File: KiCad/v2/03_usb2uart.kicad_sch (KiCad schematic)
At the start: 35 parts, among them IC301 CP2102N-A02-GQFN24R, J301 Conn_01x09_Pin, J302 Conn_01x09_Pin, J303 Conn_01x06_Pin, J304 USB_C_Receptacle_USB2.0_16P, J305 Conn_01x03_Pin, U301 USBLC6-2SC6

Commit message: Initial components placement
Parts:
- C301, C303, C304, C307, C310: footprint Capacitor_SMD:C_0603_1608Metric -> Capacitor_SMD:C_0402_1005Metric
- C302, C305, C306: footprint Capacitor_SMD:C_0805_2012Metric -> Capacitor_SMD:C_0603_1608Metric
- C311: footprint Capacitor_SMD:C_0603_1608Metric -> Capacitor_SMD:C_0402_1005Metric; now not fitted; now left out of the parts list
- SW301: now not fitted; now left out of the parts list
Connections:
- net RS485: now also J301.9 (Pin_9); no longer J301.7 (Pin_7)
- net RSTB: now also J301.7 (Pin_7); no longer J301.9 (Pin_9)
- net USB_CONN_D+: now also U301.3 (I/O2); no longer U301.1 (I/O1)
- net USB_CONN_D-: now also U301.1 (I/O1); no longer U301.3 (I/O2)
- net USB_D+: now also U301.4 (I/O2); no longer U301.6 (I/O1)
- net USB_D-: now also U301.6 (I/O1); no longer U301.4 (I/O2)
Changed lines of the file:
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@@
 	)
 	(junction
-		(at 48.26 99.06)
-		(diameter 0)
-		(color 0 0 0 0)
-	)
-	(junction
 		(at 184.15 59.69)
 		(diameter 0)
@@
 	)
 	(junction
-		(at 21.59 184.15)
+		(at 48.26 99.06)
 		(diameter 0)
 		(color 0 0 0 0)
 	)
 	(junction
-		(at 175.26 59.69)
+		(at 21.59 184.15)
 		(diameter 0)
 		(color 0 0 0 0)
 	)
 	(junction
-		(at 48.26 104.14)
+		(at 175.26 59.69)
 		(diameter 0)
 		(color 0 0 0 0)
@@
 	)
 	(junction
+		(at 48.26 101.6)
+		(diameter 0)
+		(color 0 0 0 0)
+	)
+	(junction
 		(at 151.13 39.37)
 		(diameter 0)
@@
 	(wire
 		(pts
-			(xy 53.34 99.06) (xy 48.26 99.06)
-		)
-		(stroke
-			(width 0)
-			(type default)
-		)
-	)
-	(wire
-		(pts
 			(xy 242.57 88.9) (xy 255.27 88.9)
 		)
@@
 	(wire
 		(pts
-			(xy 139.7 168.91) (xy 139.7 172.72)
+			(xy 115.57 101.6) (xy 120.65 101.6)
 		)
 		(stroke
@@
 	(wire
 		(pts
-			(xy 115.57 101.6) (xy 120.65 101.6)
+			(xy 139.7 168.91) (xy 139.7 172.72)
 		)
 		(stroke
@@
 	(wire
 		(pts
-			(xy 53.34 101.6) (xy 53.34 99.06)
-		)
-		(stroke
-			(width 0)
-			(type default)
-		)
-	)
-	(wire
-		(pts
 			(xy 41.91 78.74) (xy 48.26 78.74)
 		)
@@
 	(wire
 		(pts
+			(xy 115.57 99.06) (xy 120.65 99.06)
+		)
+		(stroke
+			(width 0)
+			(type default)
+		)
+	)
+	(wire
+		(pts
 			(xy 185.42 81.28) (xy 191.77 81.28)
 		)
@@
 	(wire
 		(pts
-			(xy 105.41 99.06) (xy 80.01 99.06)
-		)
-		(stroke
-			(width 0)
-			(type default)
-		)
-	)
-	(wire
-		(pts
-			(xy 80.01 99.06) (xy 80.01 104.14)
+			(xy 53.34 91.44) (xy 53.34 68.58)
 		)
 		(stroke
@@
 	(wire
 		(pts
-			(xy 53.34 91.44) (xy 53.34 68.58)
+			(xy 46.99 96.52) (xy 48.26 96.52)
 		)
 		(stroke
@@
 	(wire
 		(pts
-			(xy 46.99 96.52) (xy 48.26 96.52)
+			(xy 76.2 161.29) (xy 76.2 157.48)
 		)
 		(stroke
@@
 	(wire
 		(pts
-			(xy 76.2 161.29) (xy 76.2 157.48)
+			(xy 48.26 101.6) (xy 105.41 101.6)
 		)
 		(stroke
@@
 	(wire
 		(pts
-			(xy 115.57 99.06) (xy 120.65 99.06)
-		)
-		(stroke
-			(width 0)
-			(type default)
-		)
-	)
-	(wire
-		(pts
 			(xy 139.7 181.61) (xy 139.7 177.8)
 		)
@@
 	(wire
 		(pts
-			(xy 48.26 104.14) (xy 80.01 104.14)
+			(xy 48.26 99.06) (xy 105.41 99.06)
 		)
 		(stroke
@@
 	(wire
 		(pts
-			(xy 53.34 101.6) (xy 105.41 101.6)
-		)
-		(stroke
-			(width 0)
-			(type default)
-		)
-	)
-	(wire
-		(pts
 			(xy 158.75 48.26) (xy 158.75 49.53)
 		)
@@
 	)
 	(label "USB_CONN_D+"
-		(at 71.12 104.14 180)
+		(at 71.12 101.6 180)
 		(effects
 			(font
@@
 		)
 	)
-	(label "RSTB"
-		(at 247.65 45.72 0)
-		(effects
-			(font
-				(size 1.27 1.27)
-			)
-			(justify left bottom)
-		)
-	)
 	(label "WAKEUP"
 		(at 247.65 38.1 0)
@@
 	)
 	(label "USB_CONN_D-"
-		(at 71.12 101.6 180)
+		(at 71.12 99.06 180)
 		(effects
 			(font
@@
 		)
 	)
+	(label "RS485"
+		(at 247.65 45.72 0)
+		(effects
+			(font
+				(size 1.27 1.27)
+			)
+			(justify left bottom)
+		)
+	)
 	(label "DCD"
 		(at 246.38 77.47 0)
@@
 		)
 	)
+	(label "RSTB"
+		(at 247.65 40.64 0)
+		(effects
+			(font
+				(size 1.27 1.27)
+			)
+			(justify left bottom)
+		)
+	)
 	(label "RTS"
 		(at 246.38 62.23 0)
@@
 		)
 	)
-	(label "RS485"
-		(at 247.65 40.64 0)
-		(effects
-			(font
-				(size 1.27 1.27)
-			)
-			(justify left bottom)
-		)
-	)
 	(label "USB_CONN_CC1"
 		(at 69.85 64.77 180)
@@
 	(global_label "USB_D-"
 		(shape input)
-		(at 120.65 101.6 0)
+		(at 120.65 99.06 0)
 		(fields_autoplaced yes)
 		(effects
@@
 		)
 		(property "Intersheetrefs" "${INTERSHEET_REFS}"
-			(at 131.2552 101.6 0)
+			(at 131.2552 99.06 0)
 			(effects
 				(font
@@
 	(global_label "USB_D+"
 		(shape input)
-		(at 120.65 99.06 0)
+		(at 120.65 101.6 0)
 		(fields_autoplaced yes)
 		(effects
@@
 		)
 		(property "Intersheetrefs" "${INTERSHEET_REFS}"
-			(at 131.2552 99.06 0)
+			(at 131.2552 101.6 0)
 			(effects
 				(font
@@
 			)
 		)
-		(property "Footprint" "Capacitor_SMD:C_0805_2012Metric"
+		(property "Footprint" "Capacitor_SMD:C_0603_1608Metric"
 			(at 185.1152 68.58 0)
 			(effects
@@
 			)
 		)
-		(property "Footprint" "Capacitor_SMD:C_0603_1608Metric"
+		(property "Footprint" "Capacitor_SMD:C_0402_1005Metric"
 			(at 154.6352 69.85 0)
 			(effects
@@
 			)
 		)
-		(property "Footprint" "Capacitor_SMD:C_0603_1608Metric"
+		(property "Footprint" "Capacitor_SMD:C_0402_1005Metric"
 			(at 176.2252 43.18 0)
 			(effects
@@
 		(at 132.08 173.99 0)
 		(unit 1)
-		(exclude_from_sim no)
-		(in_bom yes)
-		(on_board yes)
-		(dnp no)
+		(exclude_from_sim yes)
+		(in_bom no)
+		(on_board no)
+		(dnp yes)
 		(property "Reference" "SW301"
 			(at 132.08 170.18 0)
@@
 			)
 		)
-		(property "Footprint" "Capacitor_SMD:C_0603_1608Metric"
+		(property "Footprint" "Capacitor_SMD:C_0402_1005Metric"
 			(at 95.25 87.3252 0)
 			(effects
@@
 			)
 		)
-		(property "Footprint" "Capacitor_SMD:C_0805_2012Metric"
+		(property "Footprint" "Capacitor_SMD:C_0603_1608Metric"
 			(at 185.1152 43.18 0)
 			(effects
@@
 		(at 116.84 177.8 0)
 		(unit 1)
-		(exclude_from_sim no)
-		(in_bom yes)
-		(on_board yes)
-		(dnp no)
+		(exclude_from_sim yes)
+		(in_bom no)
+		(on_board no)
+		(dnp yes)
 		(property "Reference" "C311"
 			(at 117.602 175.006 0)
@@
 			)
 		)
-		(property "Footprint" "Capacitor_SMD:C_0603_1608Metric"
+		(property "Footprint" "Capacitor_SMD:C_0402_1005Metric"
 			(at 117.8052 181.61 0)
 			(effects
@@
 			)
 		)
-		(property "Footprint" "Capacitor_SMD:C_0603_1608Metric"
+		(property "Footprint" "Capacitor_SMD:C_0402_1005Metric"
 			(at 159.7152 48.26 0)
 			(effects
@@
 			)
 		)
-		(property "Footprint" "Capacitor_SMD:C_0805_2012Metric"
+		(property "Footprint" "Capacitor_SMD:C_0603_1608Metric"
 			(at 144.4752 69.85 0)
 			(effects
@@
 			)
 		)
-		(property "Footprint" "Capacitor_SMD:C_0603_1608Metric"
+		(property "Footprint" "Capacitor_SMD:C_0402_1005Metric"
 			(at 176.2252 68.58 0)
 			(effects

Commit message: initial routing
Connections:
- net USB_CONN_D+: now also U301.1 (I/O1); no longer U301.3 (I/O2)
- net USB_CONN_D-: now also U301.3 (I/O2); no longer U301.1 (I/O1)
- net USB_D+: now also U301.6 (I/O1); no longer U301.4 (I/O2)
- net USB_D-: now also U301.4 (I/O2); no longer U301.6 (I/O1)

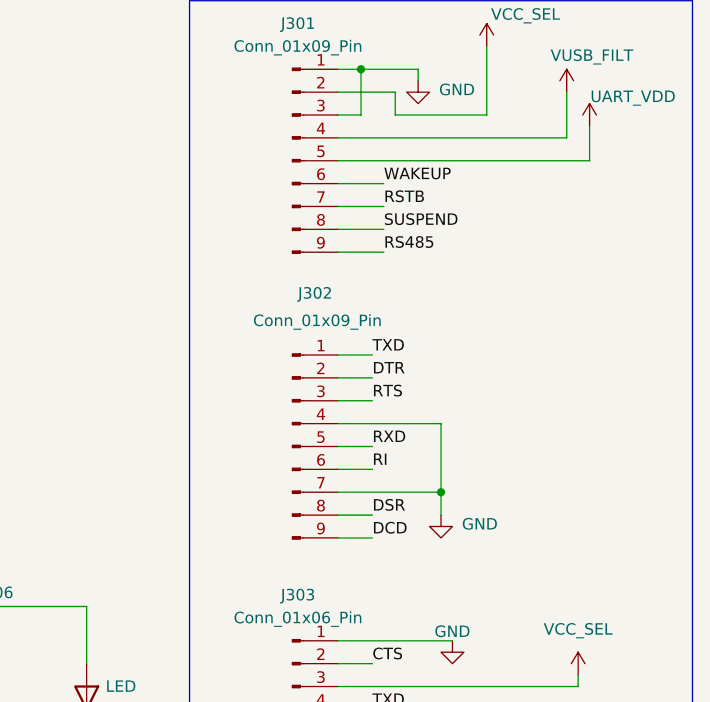
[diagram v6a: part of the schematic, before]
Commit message: Signal routing
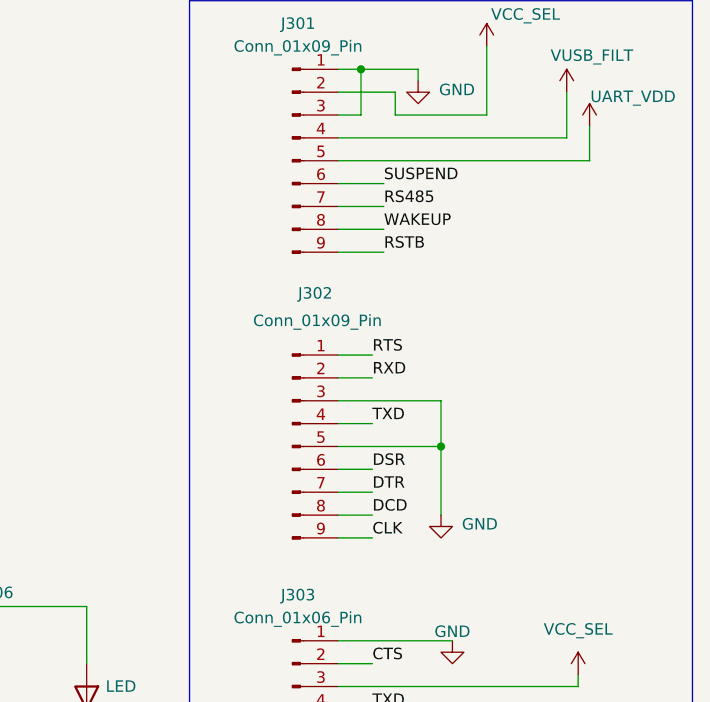
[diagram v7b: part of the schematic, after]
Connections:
- net RI is gone; now on net DSR: J302.6 (Pin_6)
- net CLK: now also J302.9 (Pin_9)
- net DCD: now also J302.8 (Pin_8); no longer J302.9 (Pin_9)
- net DSR: no longer J302.8 (Pin_8)
- net DTR: now also J302.7 (Pin_7); no longer J302.2 (Pin_2)
- net GND: now also J302.3 (Pin_3), J302.5 (Pin_5); no longer J302.4 (Pin_4), J302.7 (Pin_7)
- net RS485: now also J301.7 (Pin_7); no longer J301.9 (Pin_9)
- net RSTB: now also J301.9 (Pin_9); no longer J301.7 (Pin_7)
- net RTS: now also J302.1 (Pin_1); no longer J302.3 (Pin_3)
- net RXD: now also J302.2 (Pin_2); no longer J302.5 (Pin_5)
- net SUSPEND: now also J301.6 (Pin_6); no longer J301.8 (Pin_8)
- net TXD: now also J302.4 (Pin_4); no longer J302.1 (Pin_1)
- net WAKEUP: now also J301.8 (Pin_8); no longer J301.6 (Pin_6)
